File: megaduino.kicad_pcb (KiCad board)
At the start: 2 copper layers, 39.4 x 52.1 mm, 37 parts, among them J1 Conn_01x20_Female, J2 Conn_01x20_Female, J3 Conn_01x02_Female, J4 Conn_01x05_Male, J5 Conn_01x04_Male, J6 Conn_01x03_Male, J7 Conn_01x05_Male, J8 Conn_01x05_Male, J9 Conn_01x05_Male, Q1 2N2219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

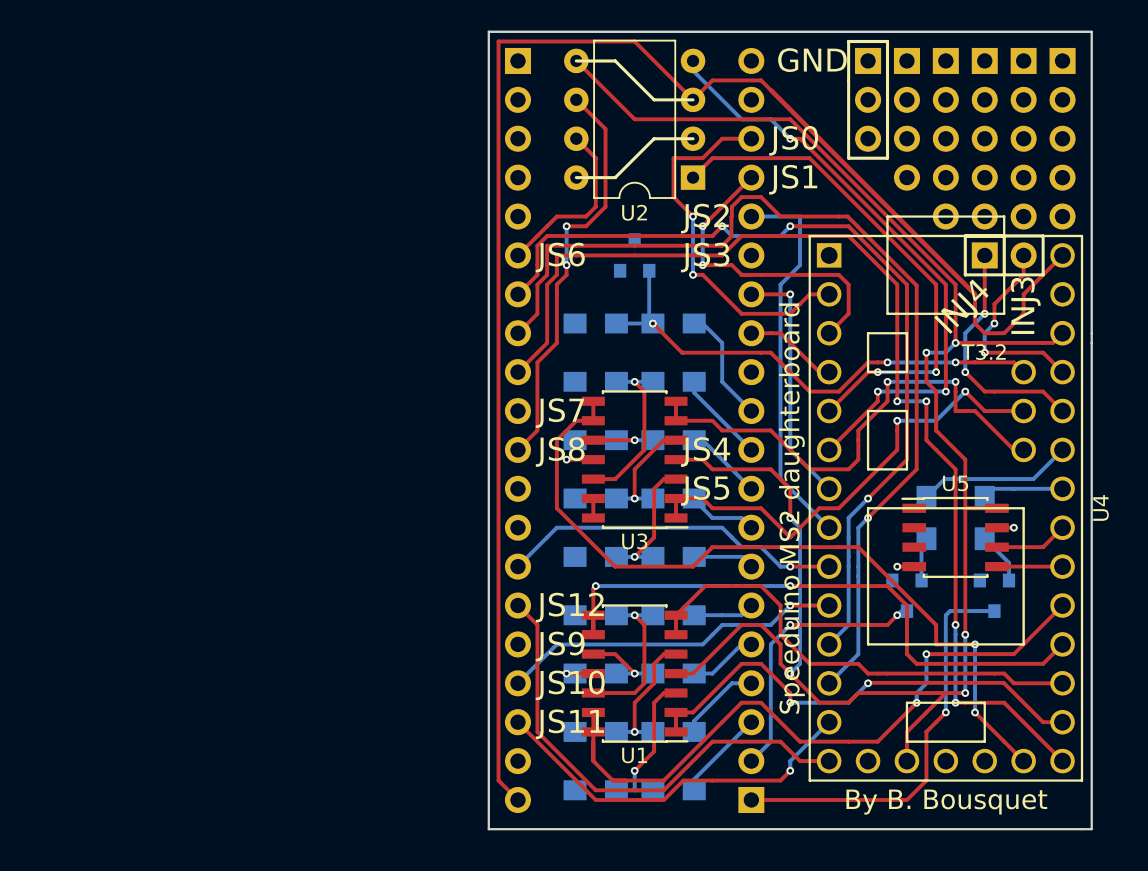
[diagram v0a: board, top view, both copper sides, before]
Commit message: updated to kicad 5.0.1 and redo all over again
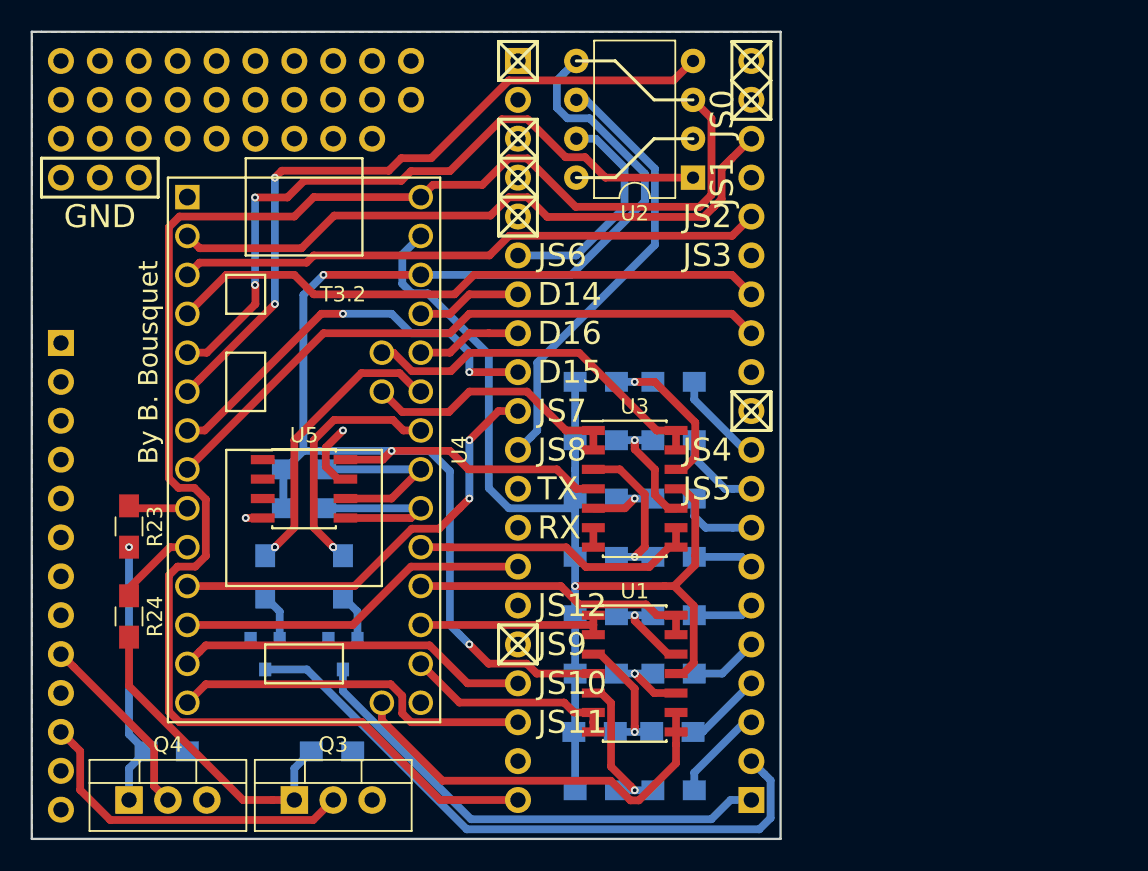
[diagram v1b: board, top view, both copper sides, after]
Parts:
- removed BZX79: D_Zener, TO_SOT_Packages_SMD:SOT-23
- added J10: Conn_01x05_Male, Pin_Headers:Pin_Header_Straight_1x05_Pitch2.54mm, B.Cu at (130.2, 73.7)
- added Q3: Q_NMOS_GDS, TO_SOT_Packages_THT:TO-220-3_Vertical, F.Cu at (135.3, 116.8)
- added Q4: Q_NMOS_GDS, TO_SOT_Packages_THT:TO-220-3_Vertical, F.Cu at (124.5, 116.8)
- added R21: R, Resistors_SMD:R_0805_HandSoldering, B.Cu at (137.7, 113.7)
- added R22: R, Resistors_SMD:R_0805_HandSoldering, B.Cu at (126.9, 113.7)
- added R23: R, Resistors_SMD:R_0805_HandSoldering, F.Cu at (124.5, 99.0)
- added R24: R, Resistors_SMD:R_0805_HandSoldering, F.Cu at (124.5, 104.9)
- J3: value Conn_01x02_Female -> Conn_01x13_Male; footprint Pin_Headers:Pin_Header_Straight_1x02_Pitch2.54mm -> Pin_Headers:Pin_Header_Straight_1x13_Pitch2.54mm
- R2: value 330k -> R
- R3: value 180k -> R
- moved J3 60.6 mm to (120.0, 87.0), turned to 180 degrees
- moved J8 60.4 mm to (120.0, 71.1), turned to 270 degrees
- moved J7 57.8 mm to (120.0, 68.6), turned to 270 degrees
- moved J5 55.5 mm to (120.0, 73.7), turned to 270 degrees
- moved J6 53.3 mm to (120.0, 76.2), turned to 270 degrees
- moved J9 52.8 mm to (132.7, 71.1), turned to 270 degrees
- moved J4 50.2 mm to (132.7, 68.6), turned to 270 degrees
- moved R4 43.3 mm to (133.3, 102.2)
- moved Q1 42.7 mm to (138.4, 107.3)
- moved U5 42.7 mm to (135.9, 96.5)
- moved U4 42.1 mm to (135.9, 94.0)
- moved Q2 42.1 mm to (133.3, 107.3)
- moved R1 42.1 mm to (138.4, 102.2)
- moved R3 27.0 mm to (135.9, 97.8)
- moved R2 21.3 mm to (135.9, 95.2)
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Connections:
- J1 pad 1: Net-(J1-Pad1) -> (no net)
- J1 pad 12: TX -> (no net)
- J1 pad 13: RX -> (no net)
- J1 pad 15: JS12 -> (no net)
- J1 pad 16: +12V -> (no net)
- J1 pad 18: JS11 -> FAN
- J1 pad 3: Net-(J1-Pad3) -> (no net)
- J1 pad 4: Net-(J1-Pad4) -> (no net)
- J1 pad 5: Net-(J1-Pad5) -> (no net)
- J2 pad 11: Net-(J2-Pad11) -> (no net)
- J2 pad 15: JS3 -> (no net)
- J2 pad 17: JS1 -> (no net)
- J2 pad 19: Net-(J2-Pad19) -> (no net)
- J2 pad 20: Net-(J2-Pad20) -> (no net)
- J3 pad 1: INJ3 -> (no net)
- J3 pad 2: INJ4 -> (no net)
- J4 pad 1: Net-(J4-Pad1) -> (no net)
- J4 pad 2: Net-(J4-Pad2) -> (no net)
- J4 pad 3: Net-(J4-Pad3) -> (no net)
- J4 pad 4: Net-(J4-Pad4) -> (no net)
- J4 pad 5: Net-(J4-Pad5) -> (no net)
- J5 pad 1: Net-(J5-Pad1) -> (no net)
- J5 pad 2: Net-(J5-Pad2) -> (no net)
- J5 pad 3: Net-(J5-Pad3) -> (no net)
- J5 pad 4: Net-(J5-Pad4) -> (no net)
- J7 pad 1: Net-(J7-Pad1) -> (no net)
- J7 pad 2: Net-(J7-Pad2) -> (no net)
- J7 pad 3: Net-(J7-Pad3) -> (no net)
- J7 pad 4: Net-(J7-Pad4) -> (no net)
- J7 pad 5: Net-(J7-Pad5) -> (no net)
- J8 pad 1: Net-(J8-Pad1) -> (no net)
- J8 pad 2: Net-(J8-Pad2) -> (no net)
- J8 pad 3: Net-(J8-Pad3) -> (no net)
- J8 pad 4: Net-(J8-Pad4) -> (no net)
- J8 pad 5: Net-(J8-Pad5) -> (no net)
- J9 pad 1: Net-(J9-Pad1) -> (no net)
- J9 pad 2: Net-(J9-Pad2) -> (no net)
- J9 pad 3: Net-(J9-Pad3) -> (no net)
- J9 pad 4: Net-(J9-Pad4) -> (no net)
- J9 pad 5: Net-(J9-Pad5) -> (no net)
- R10 pad 2: Earth -> GNDA
- R12 pad 2: Earth -> GNDA
- R14 pad 2: Earth -> GNDA
- R16 pad 2: Earth -> GNDA
- R18 pad 2: Earth -> GNDA
- R2 pad 1: Earth -> +3V3
- R2 pad 2: +3.3VA -> Net-(R2-Pad2)
- R20 pad 2: Earth -> GNDA
- R3 pad 1: +3.3VA -> +3V3
- R3 pad 2: Net-(J2-Pad11) -> Net-(R3-Pad2)
- R5 pad 1: AD0 -> AD1
- R6 pad 2: Earth -> GNDA
- R7 pad 1: AD1 -> AD0
- R8 pad 2: Earth -> GNDA
- U1 pad 11: Earth -> GNDA
- U3 pad 11: Earth -> GNDA
- U4 pad 10: IRQ1 -> INJ3
- U4 pad 11: IGN1 -> JS7
- U4 pad 12: IGN2 -> IRQ0
- U4 pad 13: JS11 -> IRQ1
- U4 pad 14: JS12 -> FAN
- U4 pad 19: A6 -> A2
- U4 pad 20: ECL -> (no net)
- U4 pad 21: A0 -> A1
- U4 pad 22: A1 -> A0
- U4 pad 23: A2 -> A3
- U4 pad 24: A3 -> A6
- U4 pad 25: Net-(U4-Pad25) -> Net-(R3-Pad2)
- U4 pad 26: Net-(U4-Pad26) -> Net-(R2-Pad2)
- U4 pad 29: INJ3 -> IGN2
- U4 pad 3: JS1 -> JS2
- U4 pad 30: INJ4 -> IGN1
- U4 pad 32: Earth -> GNDA
- U4 pad 36: A4 -> A7
- U4 pad 37: A5 -> A4
- U4 pad 4: FP -> Idle
- U4 pad 7: Idle -> ECL
- U4 pad 8: JS2 -> FP
- U4 pad 9: IRQ0 -> INJ4
- U5 pad 1: Net-(U5-Pad1) -> (no net)
- U5 pad 2: Net-(U5-Pad2) -> (no net)
- U5 pad 3: Net-(U5-Pad3) -> (no net)
- U5 pad 5: Net-(U4-Pad25) -> Net-(R3-Pad2)
- U5 pad 6: Net-(U4-Pad26) -> Net-(R2-Pad2)
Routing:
- net GNDA: track 0.00 -> 73.9 mm, vias 0 -> 1
- net IGN2: track 63.8 -> 6.88 mm, vias 1 -> 0
- net IGN1: track 56.1 -> 6.88 mm, vias 3 -> 0
- net ECL: track 71.3 -> 27.1 mm, vias 4 -> 2
- net FP: track 6.13 -> 41.6 mm
- net +3.3VA: track 33.0 -> 0.00 mm, vias 3 -> 0
- net JS12: track 31.9 -> 0.00 mm
- net A5: track 32.5 -> 1.27 mm, vias 2 -> 0
- net A6: track 50.2 -> 19.0 mm, vias 2 -> 0
- net JS7: track 0.00 -> 28.6 mm, vias 0 -> 2
- net A3: track 44.7 -> 19.4 mm, vias 2 -> 0
- net JS11: track 24.9 -> 0.00 mm, vias 1 -> 0
- net Net-(J2-Pad2): track 17.6 -> 41.9 mm, vias 2 -> 0
- net FAN: track 0.00 -> 23.8 mm
- net Idle: track 16.3 -> 39.5 mm, vias 1 -> 0
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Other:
- board size 39.4 x 52.1 mm -> 48.9 x 52.7 mm
- board text added: "D14"
- board text added: "D15"
- board text added: "D16"
- board text added: "RX"
- board text added: "TX"
- board text removed: "INJ3"
- board text removed: "INJ4"
- board text removed: "Speeduino MS2 daughterboard"

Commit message: image was too large
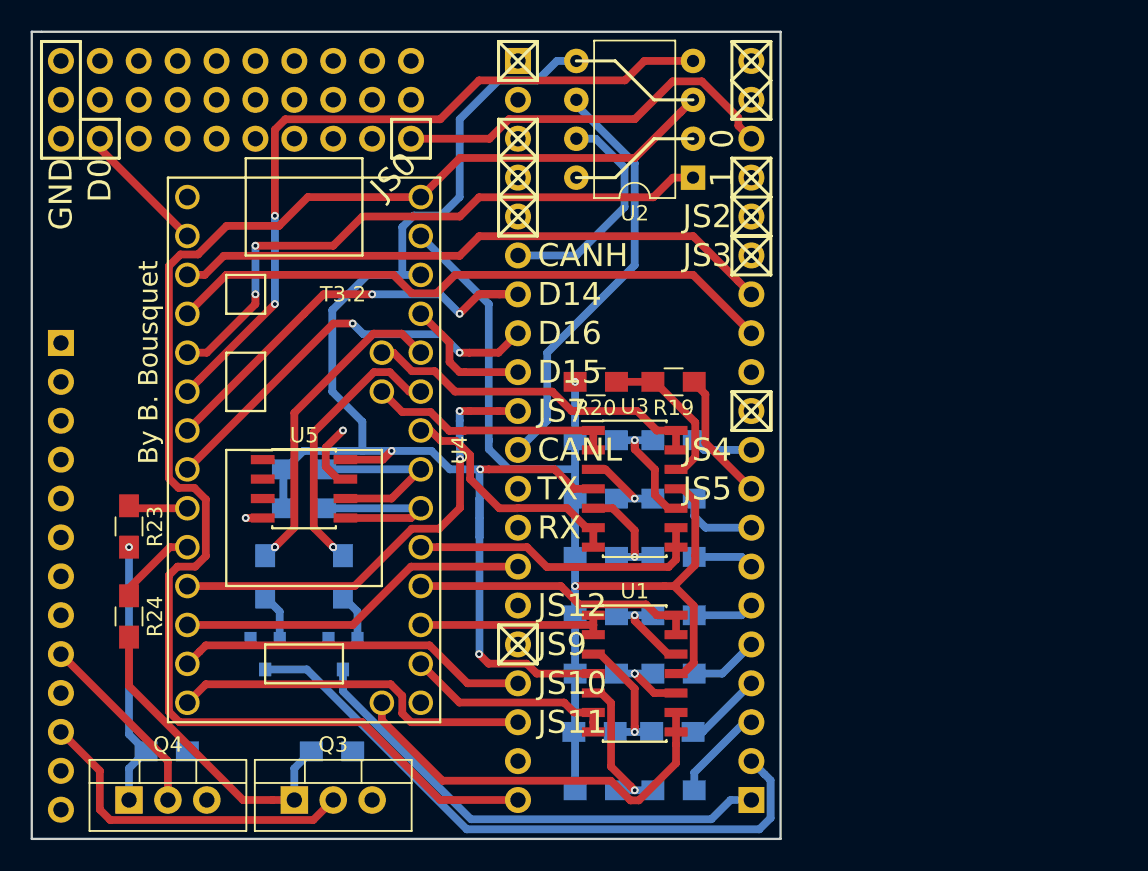
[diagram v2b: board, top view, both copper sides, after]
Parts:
- removed J10, J7, J8, J9: Conn_01x05_Male, Pin_Headers:Pin_Header_Straight_1x05_Pitch2.54mm
- J4: value Conn_01x05_Male -> Conn_01x10_Male; footprint Pin_Headers:Pin_Header_Straight_1x05_Pitch2.54mm -> Pin_Headers:Pin_Header_Straight_1x10_Pitch2.54mm
- J5: value Conn_01x04_Male -> Conn_01x10_Male; footprint Pin_Headers:Pin_Header_Straight_1x04_Pitch2.54mm -> Pin_Headers:Pin_Header_Straight_1x10_Pitch2.54mm
- J6: value Conn_01x03_Male -> Conn_01x10_Male; footprint Pin_Headers:Pin_Header_Straight_1x03_Pitch2.54mm -> Pin_Headers:Pin_Header_Straight_1x10_Pitch2.54mm
- R19, R20: moved to F.Cu
- moved J4 12.7 mm to (120.0, 68.6)
- moved J6 2.54 mm to (120.0, 73.7)
- moved J5 2.54 mm to (120.0, 71.1)
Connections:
- J2 pad 16: JS2 -> (no net)
- J4 pad 1: (no net) -> Earth
- J5 pad 1: (no net) -> Earth
- J6 pad 2: Earth -> D0
- J6 pad 3: Earth -> (no net)
- R17 pad 1: AD6 -> AD7
- R19 pad 1: AD7 -> AD6
- U1 pad 1: A0 -> A1
- U1 pad 2: A0 -> A1
- U1 pad 6: A1 -> A0
- U1 pad 7: A1 -> A0
- U3 pad 1: A4 -> A5
- U3 pad 13: A7 -> A6
- U3 pad 14: A7 -> A6
- U3 pad 2: A4 -> A5
- U3 pad 3: Net-(R13-Pad2) -> Net-(R15-Pad2)
- U3 pad 5: Net-(R15-Pad2) -> Net-(R13-Pad2)
- U3 pad 6: A5 -> A4
- U3 pad 7: A5 -> A4
- U3 pad 8: A6 -> A7
- U3 pad 9: A6 -> A7
- U4 pad 2: JS0 -> D0
- U4 pad 21: A1 -> A0
- U4 pad 22: A0 -> A1
- U4 pad 24: A6 -> A7
- U4 pad 27: INJ1 -> A4
- U4 pad 28: INJ2 -> INJ1
- U4 pad 29: IGN2 -> INJ2
- U4 pad 3: JS2 -> Idle
- U4 pad 30: IGN1 -> ECL
- U4 pad 36: A7 -> A6
- U4 pad 37: A4 -> A5
- U4 pad 4: Idle -> FP
- U4 pad 7: ECL -> IGN1
- U4 pad 8: FP -> IGN2
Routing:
- net JS2: track 38.4 -> 0.00 mm
- net IGN1: track 6.88 -> 28.7 mm, vias 0 -> 2
- net IGN2: track 6.88 -> 26.9 mm, vias 0 -> 2
- net ECL: track 27.1 -> 8.67 mm, vias 2 -> 0
- net JS0: track 43.3 -> 25.6 mm
- net A5: track 1.27 -> 16.2 mm
- net +3V3: track 100.6 -> 88.8 mm
- net +5V: track 105.7 -> 96.3 mm
- net D0: track 0.00 -> 8.72 mm
- net Net-(U2-Pad1): track 45.0 -> 40.0 mm
- net GNDA: track 73.9 -> 69.8 mm, vias 1 -> 2
- net A7: track 23.6 -> 19.5 mm
- net A6: track 19.0 -> 22.6 mm
- net Net-(R13-Pad2): track 10.8 -> 7.41 mm
- net AD6: track 5.72 -> 8.56 mm
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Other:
- board text added: "0"
- board text added: "1"
- board text added: "CANH"
- board text added: "CANL"
- board text added: "D0"
- board text removed: "JS1"
- board text removed: "JS6"
- board text removed: "JS8"

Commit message: version pas mal finale
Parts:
- added D1: LED, LEDs:LED_0805_HandSoldering, F.Cu at (123.8, 90.8)
- added D2: LED, LEDs:LED_0805_HandSoldering, F.Cu at (123.8, 94.0)
- added D3: LED, LEDs:LED_0805_HandSoldering, F.Cu at (123.8, 97.2)
- added D4: LED, LEDs:LED_0805_HandSoldering, F.Cu at (123.8, 100.6)
- added D5: LED, LEDs:LED_0805_HandSoldering, F.Cu at (155.0, 83.8)
- added D6: LED, LEDs:LED_0805_HandSoldering, F.Cu at (155.0, 86.4)
- added JP1: Jumper, Resistors_SMD:R_0805_HandSoldering, B.Cu at (146.7, 111.8)
- added R25: R, Resistors_SMD:R_0805_HandSoldering, F.Cu at (124.5, 83.8)
- added R26: R, Resistors_SMD:R_0805_HandSoldering, F.Cu at (160.1, 85.7)
- Q3, Q4: footprint TO_SOT_Packages_THT:TO-220-3_Vertical -> TO_SOT_Packages_THT:TO-251_IPAK_Vertical
- R19, R20: moved to B.Cu
- R2, R3: value R -> 1k; moved to F.Cu
- R21, R22: value R -> 100k
- R23: value R -> 1k; moved to B.Cu
- R24: value R -> 1k
- U2: footprint Housings_DIP:DIP-8_W7.62mm -> Housings_SOIC:SOIC-8_3.9x4.9mm_Pitch1.27mm
- moved R23 16.5 mm to (132.1, 113.7)
- moved Q3 10.8 mm to (124.5, 116.8)
- moved Q4 10.8 mm to (135.3, 116.8)
- moved R21 10.7 mm to (127.0, 113.7)
- moved R22 10.2 mm to (137.1, 113.7)
- moved R2 6.48 mm to (134.6, 101.6), turned to 90 degrees
- moved U2 5.85 mm to (157.5, 71.8), turned to 0 degrees
- moved Q1 5.08 mm to (133.3, 107.3)
- moved Q2 5.08 mm to (138.4, 107.3)
- moved R1 5.08 mm to (133.3, 102.2)
- moved R4 5.08 mm to (138.4, 102.2)
- moved R3 4.02 mm to (137.2, 101.6), turned to 90 degrees
- moved U5 1.27 mm to (135.9, 95.2)
- moved R24 1.19 mm to (124.5, 106.0)
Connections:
- J1 pad 15: (no net) -> JS12
- U4 pad 10: INJ3 -> INJ4
- U4 pad 20: (no net) -> Net-(JP1-Pad2)
- U4 pad 28: INJ1 -> ECL
- U4 pad 29: INJ2 -> IGN2
- U4 pad 30: ECL -> IGN1
- U4 pad 7: IGN1 -> INJ1
- U4 pad 8: IGN2 -> INJ2
- U4 pad 9: INJ4 -> INJ3
- U5 pad 1: (no net) -> Earth
- U5 pad 2: (no net) -> Earth
- U5 pad 3: (no net) -> Earth
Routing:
- net Earth: track 5.56 -> 28.3 mm
- net IGN1: track 28.7 -> 10.7 mm, vias 2 -> 0
- net IGN2: track 26.9 -> 10.7 mm, vias 2 -> 0
- net Net-(D1-Pad1): track 0.00 -> 15.7 mm
- net INJ4: track 3.88 -> 17.6 mm
- net Net-(J3-Pad11): track 22.2 -> 9.17 mm
- net Net-(U2-Pad4): track 48.6 -> 36.1 mm
- net Net-(Q4-Pad1): track 17.4 -> 6.58 mm, vias 1 -> 0
- net Net-(Q3-Pad1): track 20.7 -> 10.4 mm, vias 0 -> 1
- net Net-(J2-Pad2): track 41.9 -> 31.6 mm, vias 0 -> 1
- net Net-(J3-Pad9): track 12.4 -> 21.5 mm
- net +3V3: track 88.8 -> 97.6 mm, vias 3 -> 4
- net JS12: track 0.00 -> 7.63 mm
- net +5V: track 96.3 -> 89.2 mm
- net INJ3: track 5.42 -> 11.2 mm
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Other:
- board text added: "12V"
- board text added: "2"
- board text added: "3"
- board text added: "4"
- board text added: "IGN"
- board text added: "INJ"
- board text removed: "0"
- board text removed: "CANH"
- board text removed: "CANL"
- board text removed: "D14"
- board text removed: "D15"
- board text removed: "D16"
- board text removed: "JS10"
- board text removed: "JS11"
- board text removed: "JS12"
- board text removed: "JS2"
- board text removed: "JS3"
- board text removed: "JS4"
- board text removed: "JS5"
- board text removed: "JS7"
- board text removed: "JS9"
- board text removed: "RX"
- board text removed: "TX"

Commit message: js7 in now on proto area
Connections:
- J2 pad 19: (no net) -> Net-(J2-Pad19)
- J2 pad 20: (no net) -> Net-(J2-Pad19)
- J5 pad 10: Earth -> JS7
- J6 pad 2: D0 -> D7
- J6 pad 3: (no net) -> D0
- U4 pad 10: INJ4 -> INJ3
- U4 pad 11: JS7 -> INJ4
- U4 pad 3: Idle -> D7
- U4 pad 4: FP -> Idle
- U4 pad 7: INJ1 -> FP
- U4 pad 8: INJ2 -> INJ1
- U4 pad 9: INJ3 -> INJ2
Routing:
- net D7: track 0.00 -> 11.3 mm
- net JS7: track 30.7 -> 38.9 mm, vias 0 -> 1
- net CANL: track 32.4 -> 27.5 mm
- net FP: track 40.5 -> 45.2 mm
- net INJ4: track 17.6 -> 15.0 mm
- net Net-(J2-Pad19): track 0.00 -> 2.54 mm
- net Net-(U2-Pad1): track 37.3 -> 35.3 mm
- net +5V: track 89.2 -> 87.8 mm
- net JS0: track 27.4 -> 28.6 mm
- net Idle: track 40.7 -> 41.7 mm
- net D0: track 8.72 -> 7.67 mm
- net INJ1: track 17.4 -> 16.5 mm
- net Net-(U2-Pad4): track 36.1 -> 35.3 mm
- net Net-(J3-Pad9): track 21.5 -> 22.1 mm
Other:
- board text added: "D7"
- board text added: "JS7"
